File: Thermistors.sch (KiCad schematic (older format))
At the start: 0 parts

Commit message: Added thermistor schem
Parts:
- added C? (x8): 2.2uF, symbol Device:C_Small
- added D? (x16): S_D, symbol Device:D_Schottky_Small
- added J? (x8): Conn_01x02, symbol Connector_Generic:Conn_01x02
- added R? (x8): 4.7k, symbol Device:R_Small_US
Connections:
- new net +3.3VA: D?.1 (K), D?.1 (K), D?.1 (K), D?.1 (K), D?.1 (K), D?.1 (K), D?.1 (K), D?.1 (K), R?.1, R?.1, R?.1, R?.1, R?.1, R?.1, R?.1, R?.1
- new net BED_THERM: C?.1, D?.1 (K), D?.2 (A), J?.1 (Pin_1), R?.2
- new net CHAMBER_THERM: C?.1, D?.1 (K), D?.2 (A), J?.1 (Pin_1), R?.2
- new net GND: C?.2, C?.2, C?.2, C?.2, C?.2, C?.2, C?.2, C?.2, D?.2 (A), D?.2 (A), D?.2 (A), D?.2 (A), D?.2 (A), D?.2 (A), D?.2 (A), D?.2 (A), J?.2 (Pin_2), J?.2 (Pin_2), J?.2 (Pin_2), J?.2 (Pin_2), J?.2 (Pin_2), J?.2 (Pin_2), J?.2 (Pin_2), J?.2 (Pin_2)
- new net THERM0: C?.1, D?.1 (K), D?.2 (A), J?.1 (Pin_1), R?.2
- new net THERM1: C?.1, D?.1 (K), D?.2 (A), J?.1 (Pin_1), R?.2
- new net THERM2: C?.1, D?.1 (K), D?.2 (A), J?.1 (Pin_1), R?.2
- new net THERM3: C?.1, D?.1 (K), D?.2 (A), J?.1 (Pin_1), R?.2
- new net THERM4: C?.1, D?.1 (K), D?.2 (A), J?.1 (Pin_1), R?.2
- new net THERM5: C?.1, D?.1 (K), D?.2 (A), J?.1 (Pin_1), R?.2

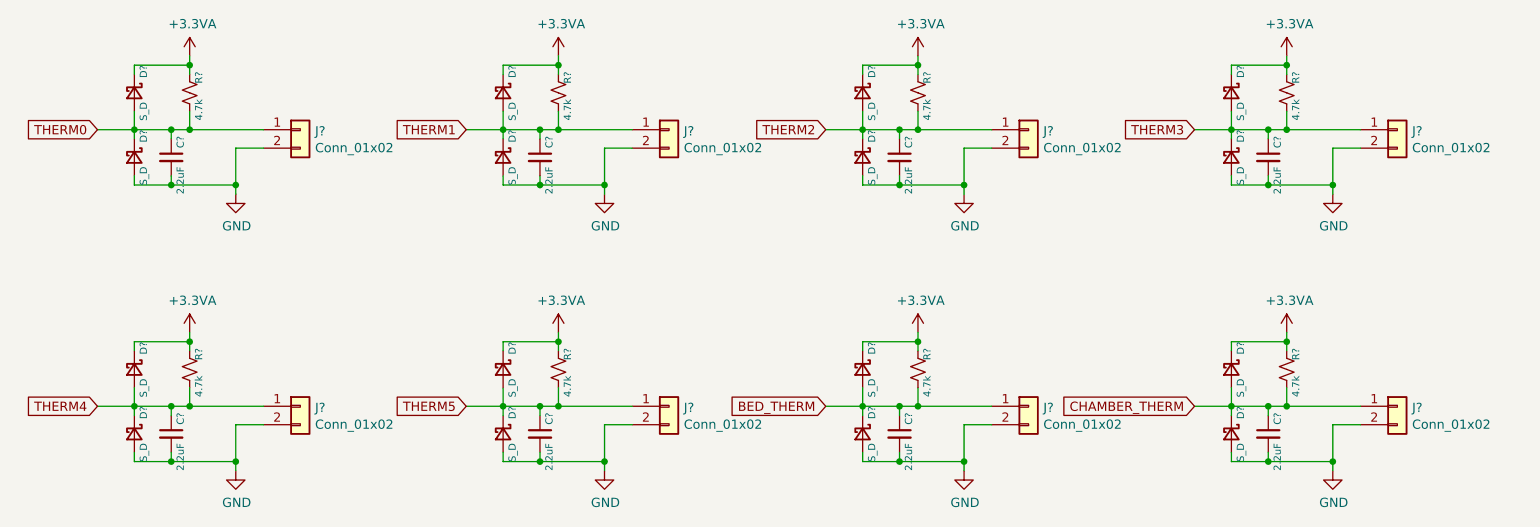
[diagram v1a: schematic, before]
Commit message: added raspberry pi header
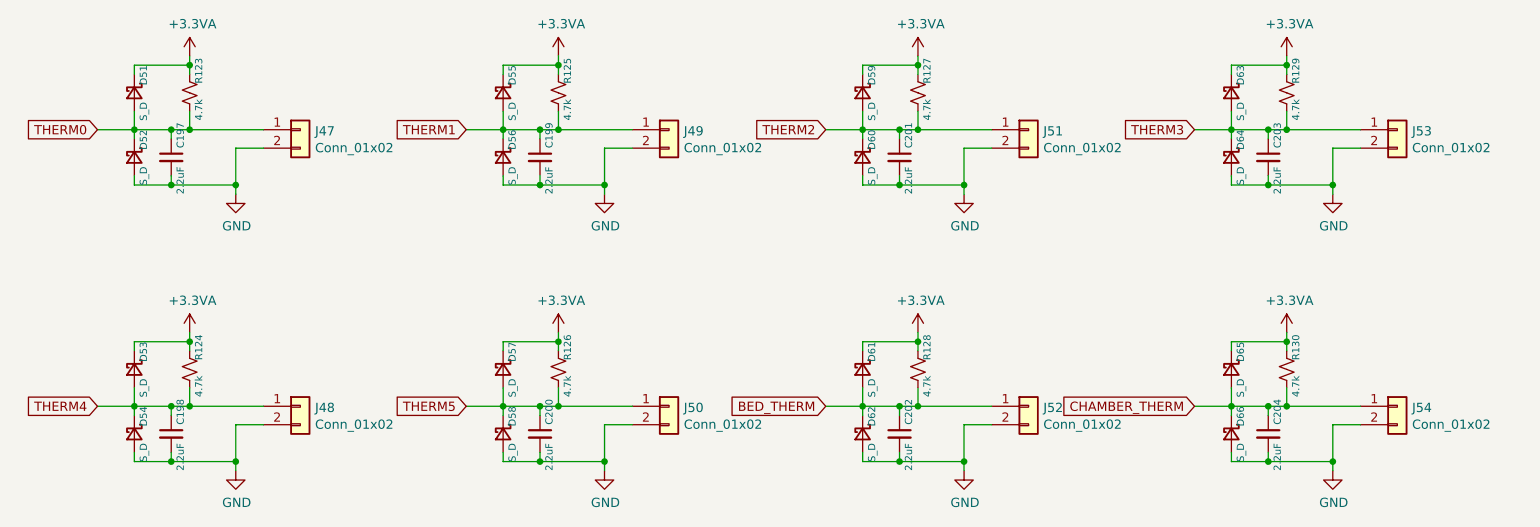
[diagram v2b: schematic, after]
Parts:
- gave numbers to parts that had none: 40

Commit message: associated more footprints
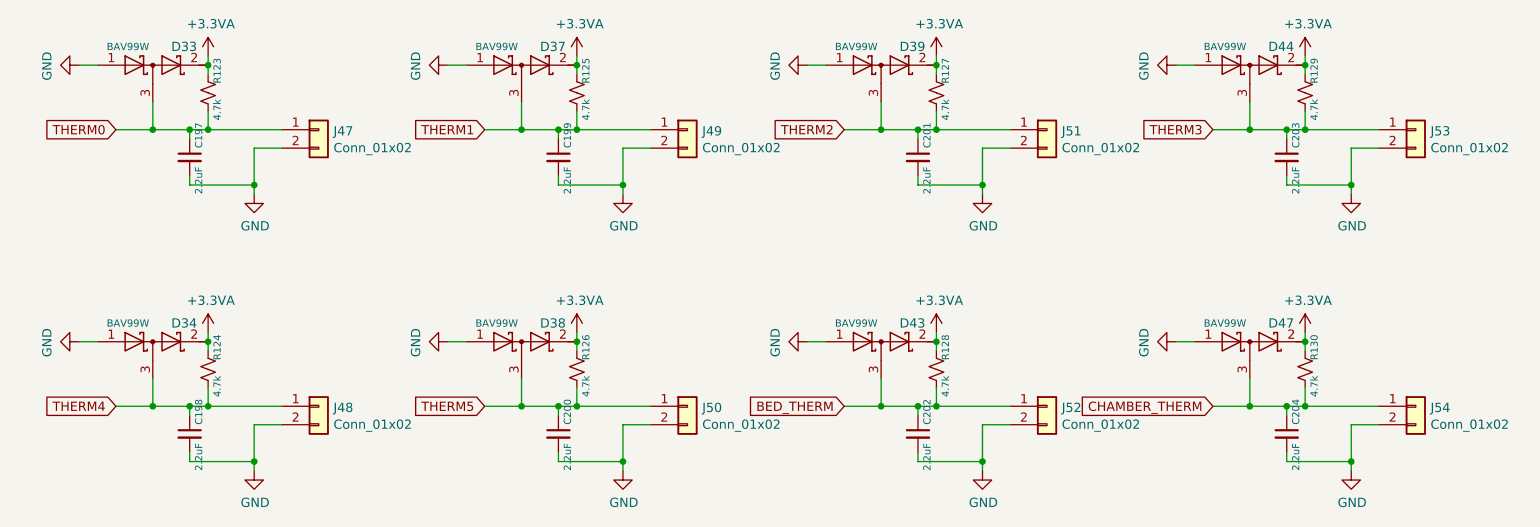
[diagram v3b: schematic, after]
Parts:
- removed D51, D52, D53, D54, D55, D56, D57, D58, D59, D60, D61, D62, D63, D64, D65, D66: S_D, symbol Device:D_Schottky_Small
- added D33, D34, D37, D38, D39, D43, D44, D47: BAV99W, Package_TO_SOT_SMD:SOT-323_SC-70_Handsoldering, symbol Device:D_Schottky_x2_Serial_AKC
- C197, C198, C199, C200, C201, C202, C203, C204: footprint (none) -> Capacitor_SMD:C_0603_1608Metric_Pad1.05x0.95mm_HandSolder
- J47, J48, J49, J50, J51, J52, J53, J54: footprint (none) -> Connector_Molex:Molex_KK-254_AE-6410-02A_1x02_P2.54mm_Vertical
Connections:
- net +3.3VA: now also D33.2 (K), D34.2 (K), D37.2 (K), D38.2 (K), D39.2 (K), D43.2 (K), D44.2 (K), D47.2 (K)
- net BED_THERM: now also D43.3 (common)
- net CHAMBER_THERM: now also D47.3 (common)
- net GND: now also D33.1 (A), D34.1 (A), D37.1 (A), D38.1 (A), D39.1 (A), D43.1 (A), D44.1 (A), D47.1 (A)
- net THERM0: now also D33.3 (common)
- net THERM1: now also D37.3 (common)
- net THERM2: now also D39.3 (common)
- net THERM3: now also D44.3 (common)
- net THERM4: now also D34.3 (common)
- net THERM5: now also D38.3 (common)
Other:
- moved on the sheet: C197, C198, C199, C200, C201, C202, C203, C204, J47, J48, J49, J50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

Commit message: Added more footprints
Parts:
- R123, R124, R125, R126, R127, R128, R129, R130: footprint (none) -> Resistor_SMD:R_0603_1608Metric_Pad1.05x0.95mm_HandSolder
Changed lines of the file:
@@
 $Descr A4 11693 8268
 encoding utf-8
-Sheet 7 9
+Sheet 6 9
 Title ""
 Date "2020-10-23"
@@
 F 0 "R123" V 2850 2850 39  0000 L CNN
 F 1 "4.7k" V 2850 2650 39  0000 L CNN
-F 2 "" H 2800 2800 50  0001 C CNN
+F 2 "Resistor_SMD:R_0603_1608Metric_Pad1.05x0.95mm_HandSolder" H 2800 2800 50  0001 C CNN
 F 3 "~" H 2800 2800 50  0001 C CNN
 	1    2800 2800
@@
 F 0 "R125" V 4850 2850 39  0000 L CNN
 F 1 "4.7k" V 4850 2650 39  0000 L CNN
-F 2 "" H 4800 2800 50  0001 C CNN
+F 2 "Resistor_SMD:R_0603_1608Metric_Pad1.05x0.95mm_HandSolder" H 4800 2800 50  0001 C CNN
 F 3 "~" H 4800 2800 50  0001 C CNN
 	1    4800 2800
@@
 F 0 "R127" V 6800 2850 39  0000 L CNN
 F 1 "4.7k" V 6800 2650 39  0000 L CNN
-F 2 "" H 6750 2800 50  0001 C CNN
+F 2 "Resistor_SMD:R_0603_1608Metric_Pad1.05x0.95mm_HandSolder" H 6750 2800 50  0001 C CNN
 F 3 "~" H 6750 2800 50  0001 C CNN
 	1    6750 2800
@@
 F 0 "R129" V 8800 2850 39  0000 L CNN
 F 1 "4.7k" V 8800 2650 39  0000 L CNN
-F 2 "" H 8750 2800 50  0001 C CNN
+F 2 "Resistor_SMD:R_0603_1608Metric_Pad1.05x0.95mm_HandSolder" H 8750 2800 50  0001 C CNN
 F 3 "~" H 8750 2800 50  0001 C CNN
 	1    8750 2800
@@
 F 0 "R124" V 2850 4350 39  0000 L CNN
 F 1 "4.7k" V 2850 4150 39  0000 L CNN
-F 2 "" H 2800 4300 50  0001 C CNN
+F 2 "Resistor_SMD:R_0603_1608Metric_Pad1.05x0.95mm_HandSolder" H 2800 4300 50  0001 C CNN
 F 3 "~" H 2800 4300 50  0001 C CNN
 	1    2800 4300
@@
 F 0 "R126" V 4850 4350 39  0000 L CNN
 F 1 "4.7k" V 4850 4150 39  0000 L CNN
-F 2 "" H 4800 4300 50  0001 C CNN
+F 2 "Resistor_SMD:R_0603_1608Metric_Pad1.05x0.95mm_HandSolder" H 4800 4300 50  0001 C CNN
 F 3 "~" H 4800 4300 50  0001 C CNN
 	1    4800 4300
@@
 F 0 "R128" V 6800 4350 39  0000 L CNN
 F 1 "4.7k" V 6800 4150 39  0000 L CNN
-F 2 "" H 6750 4300 50  0001 C CNN
+F 2 "Resistor_SMD:R_0603_1608Metric_Pad1.05x0.95mm_HandSolder" H 6750 4300 50  0001 C CNN
 F 3 "~" H 6750 4300 50  0001 C CNN
 	1    6750 4300
@@
 F 0 "R130" V 8800 4350 39  0000 L CNN
 F 1 "4.7k" V 8800 4150 39  0000 L CNN
-F 2 "" H 8750 4300 50  0001 C CNN
+F 2 "Resistor_SMD:R_0603_1608Metric_Pad1.05x0.95mm_HandSolder" H 8750 4300 50  0001 C CNN
 F 3 "~" H 8750 4300 50  0001 C CNN
 	1    8750 4300
